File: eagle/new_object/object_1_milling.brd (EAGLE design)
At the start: 56.6 x 34.8 mm, 13 parts, among them U1 GY-521MPU6050

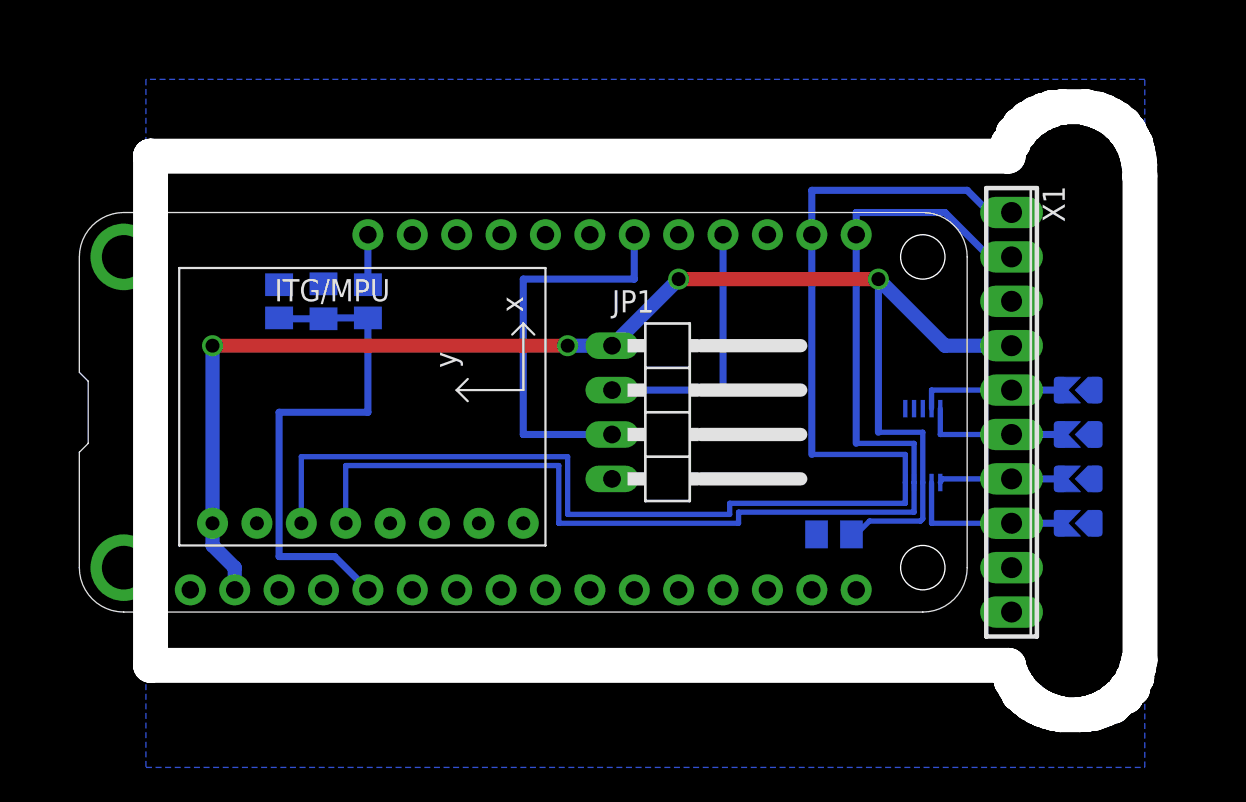
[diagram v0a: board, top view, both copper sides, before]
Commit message: Change switch to pin 23, clean the mess git did with the files
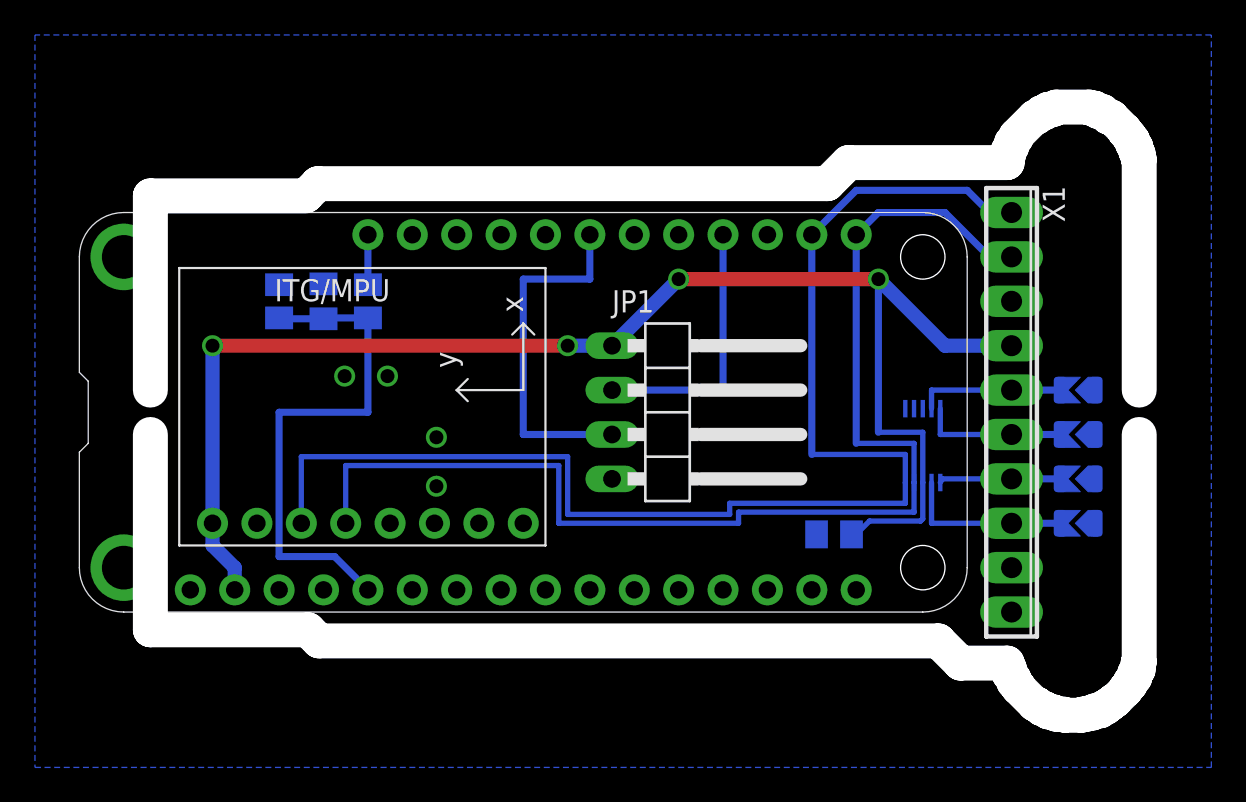
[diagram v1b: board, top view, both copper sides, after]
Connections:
- net BTN: now also MS1.23; no longer MS1.22
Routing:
- net BTN: track 22.9 -> 20.3 mm
- net SCL: track 77.5 -> 76.0 mm
- net SDA: track 70.2 -> 69.4 mm
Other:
- outline, holes or cut-outs redrawn
